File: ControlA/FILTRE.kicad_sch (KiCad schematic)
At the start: 0 parts

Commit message: usb control
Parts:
- added C? (x3): 100n, symbol Device:C
- added C? (x3): 4n7, symbol Device:C
- added R? (x3): 2K2, symbol Device:R
- added R? (x3): 10K, symbol Device:R
- added U?: B06B-PARK-1_(LF)(SN), symbol B06B-PARK-1(LF)(SN):B06B-PARK-1_(LF)(SN)
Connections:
- new net: C?.1, R?.2 (x3)
- new net +3V3: C?.1, C?.1, C?.1, R?.1, R?.1, R?.1
- new net +5V: U?.6
- new net GND: C?.2, C?.2, C?.2, C?.2, C?.2, C?.2, U?.1
- new net HALL_1_IN: R?.1, U?.4
- new net HALL_1_OUT: R?.2
- new net HALL_2_IN: R?.1, U?.3
- new net HALL_2_OUT: R?.2
- new net HALL_3_IN: R?.1, U?.2
- new net HALL_3_OUT: R?.2
- new net TEMP_IN: U?.5
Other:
- note added: "FILTRE"
- note added: "HALL ENCODER INPUT"
- note added: "Hall_1 FILTRE"
- note added: "Hall_2 FILTRE"
- note added: "Hall_3 FILTRE"

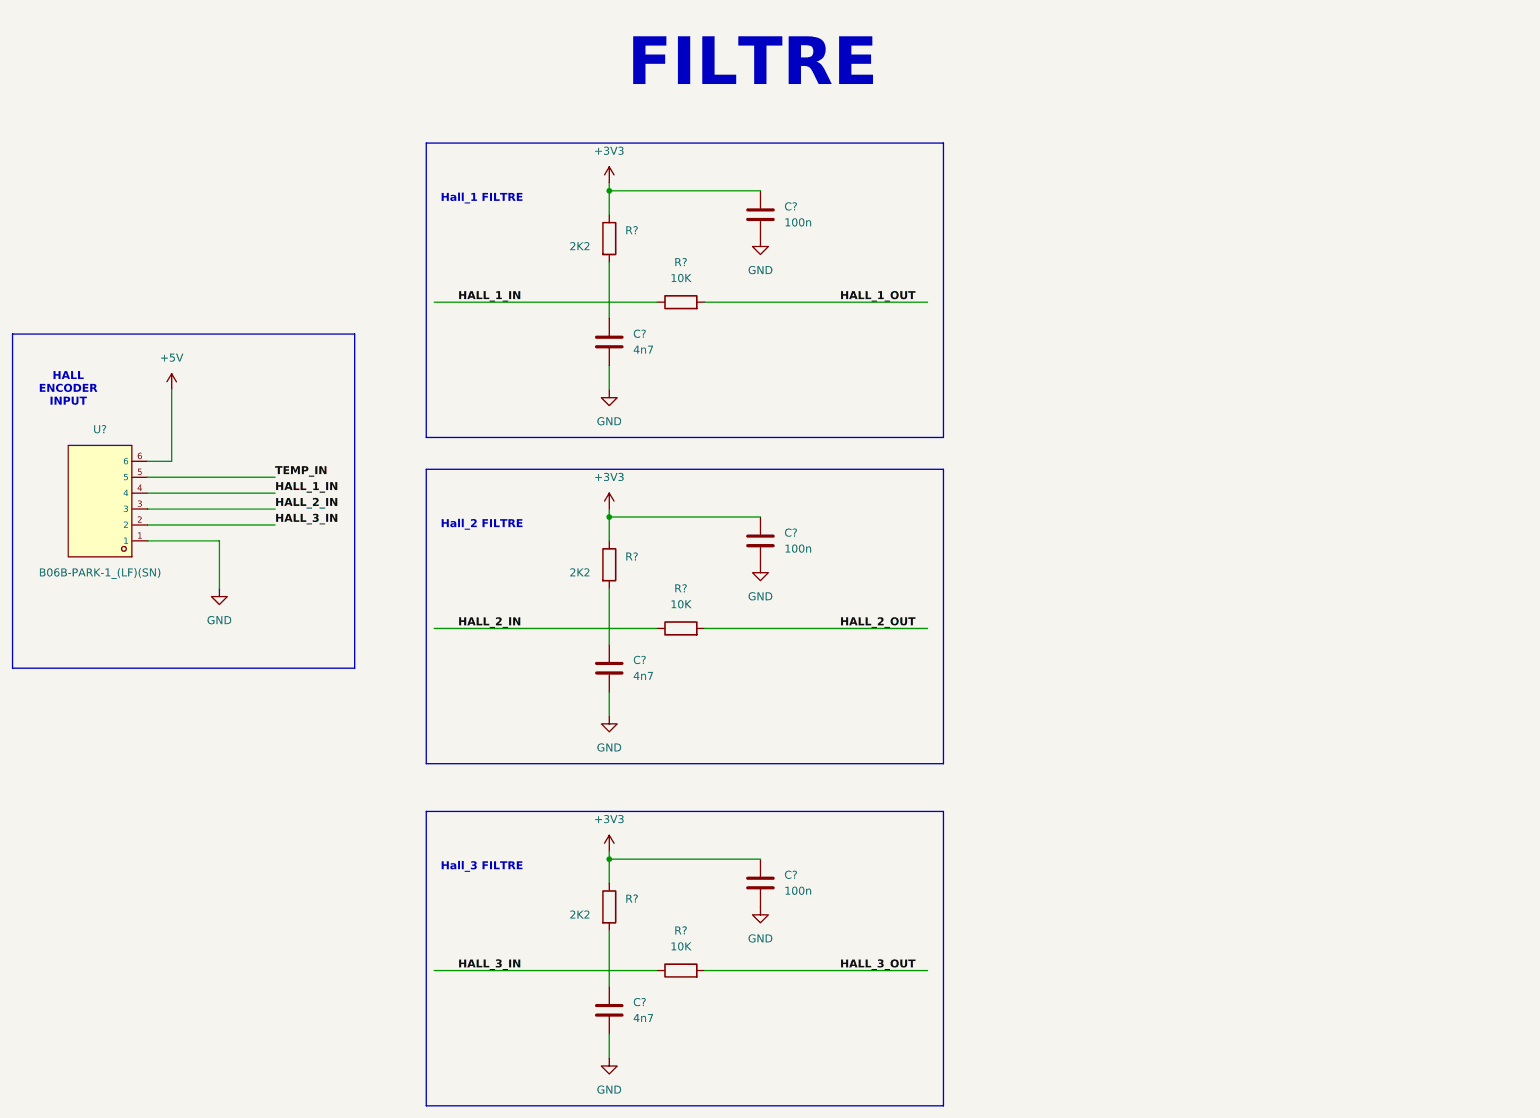
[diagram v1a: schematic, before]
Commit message: final shema symbole
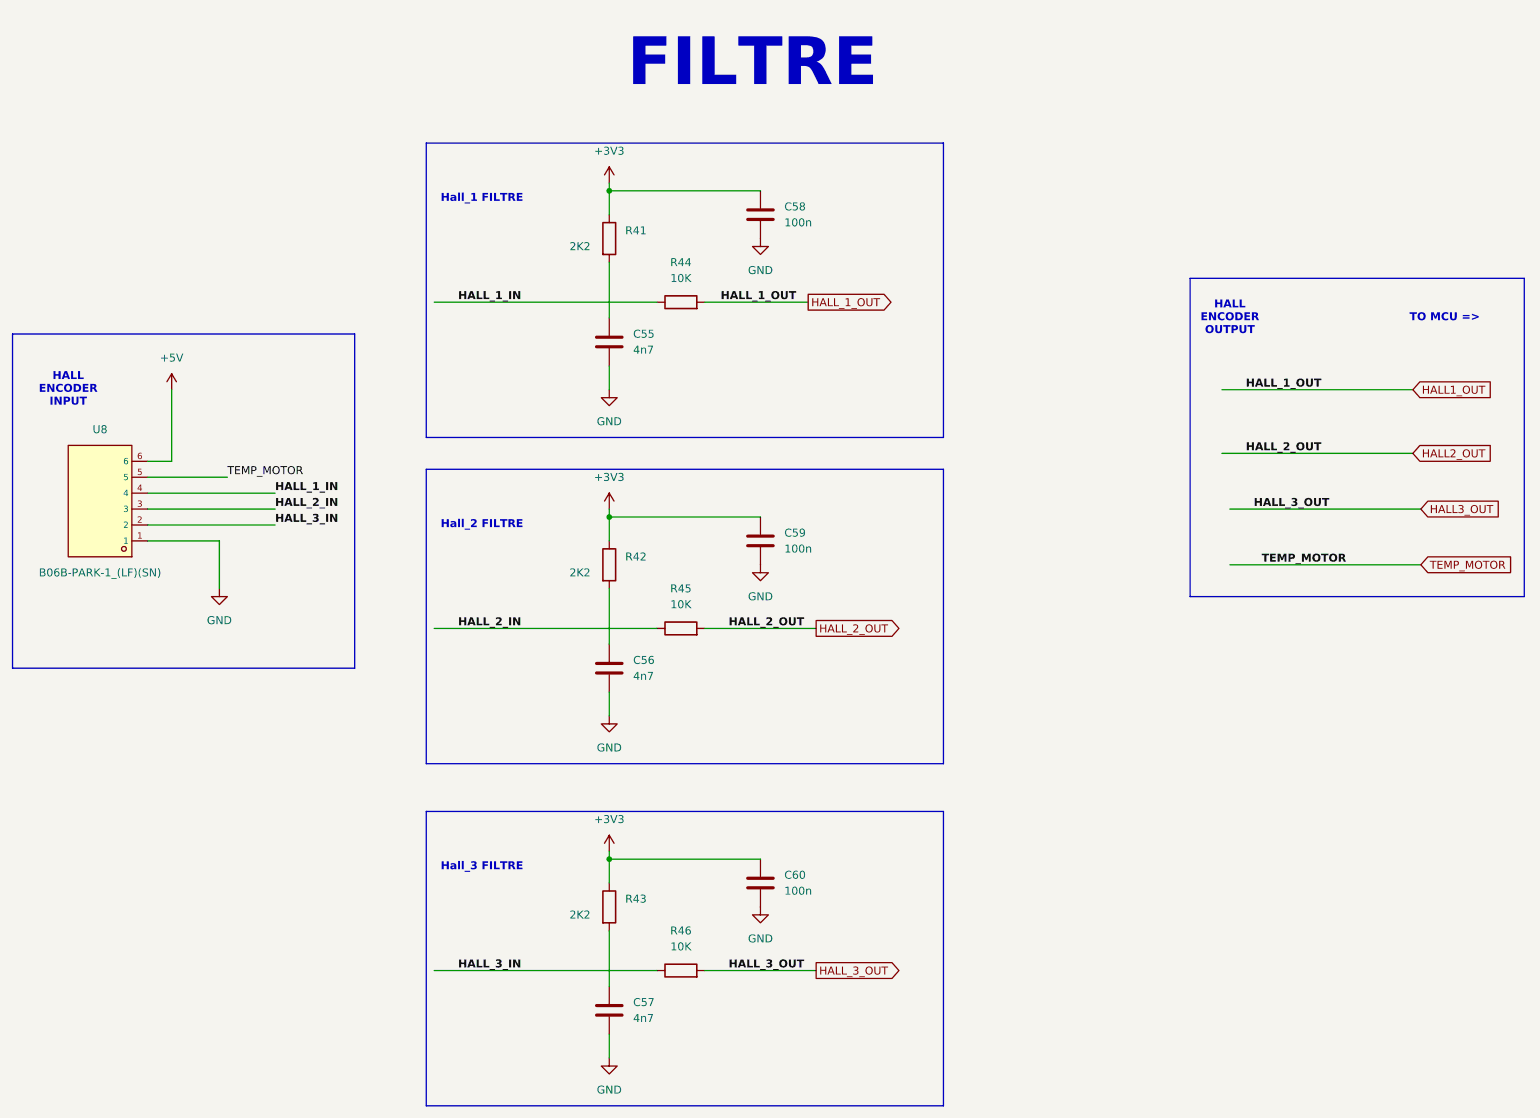
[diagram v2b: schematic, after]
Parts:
- C55, C56, C57, C58, C59, C60: renamed from C?; footprint (none) -> Capacitor_SMD:C_0805_2012Metric
- R41, R42, R43, R44, R45, R46: renamed from R?; footprint (none) -> Resistor_SMD:R_0805_2012Metric
- U8: renamed from U?; footprint (none) -> footprint:CONN-TH_B06B-PARK-1-LF-SN
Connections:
- net HALL_1_OUT renamed HALL1_OUT
- net HALL_2_OUT renamed HALL2_OUT
- net HALL_3_OUT renamed HALL3_OUT
- net TEMP_IN renamed TEMP_MOTOR
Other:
- note added: "HALL ENCODER OUTPUT"
- note added: "TO MCU =>"

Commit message: CHANGE V11
change v1
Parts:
- C55, C56, C57, C58, C59, C60: footprint Capacitor_SMD:C_0805_2012Metric -> Capacitor_SMD:C_0603_1608Metric
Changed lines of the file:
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@@
 			)
 		)
-		(property "Footprint" "Capacitor_SMD:C_0805_2012Metric"
+		(property "Footprint" "Capacitor_SMD:C_0603_1608Metric"
 			(at 145.7452 48.26 0)
 			(effects
@@
 			)
 		)
-		(property "Footprint" "Capacitor_SMD:C_0805_2012Metric"
+		(property "Footprint" "Capacitor_SMD:C_0603_1608Metric"
 			(at 121.6152 175.26 0)
 			(effects
@@
 			)
 		)
-		(property "Footprint" "Capacitor_SMD:C_0805_2012Metric"
+		(property "Footprint" "Capacitor_SMD:C_0603_1608Metric"
 			(at 145.7452 154.94 0)
 			(effects
@@
 			)
 		)
-		(property "Footprint" "Capacitor_SMD:C_0805_2012Metric"
+		(property "Footprint" "Capacitor_SMD:C_0603_1608Metric"
 			(at 121.6152 68.58 0)
 			(effects
@@
 			)
 		)
-		(property "Footprint" "Capacitor_SMD:C_0805_2012Metric"
+		(property "Footprint" "Capacitor_SMD:C_0603_1608Metric"
 			(at 145.7452 100.33 0)
 			(effects
@@
 			)
 		)
-		(property "Footprint" "Capacitor_SMD:C_0805_2012Metric"
+		(property "Footprint" "Capacitor_SMD:C_0603_1608Metric"
 			(at 121.6152 120.65 0)
 			(effects
